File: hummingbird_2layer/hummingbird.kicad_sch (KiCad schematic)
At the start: 42 parts, among them J1 USB_C_Receptacle_USB2.0_16P, J2 srv1, J3 srv2, J4 halleffect, J5 Conn_01x06, J6 Conn_01x02, J7 Conn_01x02, J8 PWR_IN, J9 Conn_02x02_Counter_Clockwise, Q1 AO3400A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

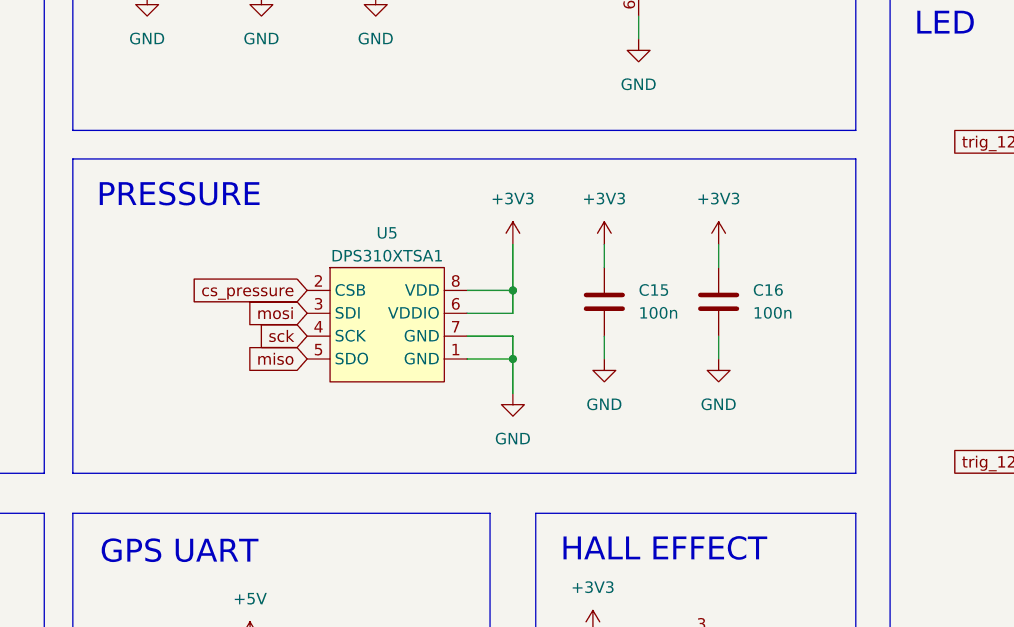
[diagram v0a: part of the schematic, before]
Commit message: backup before replacing sensor
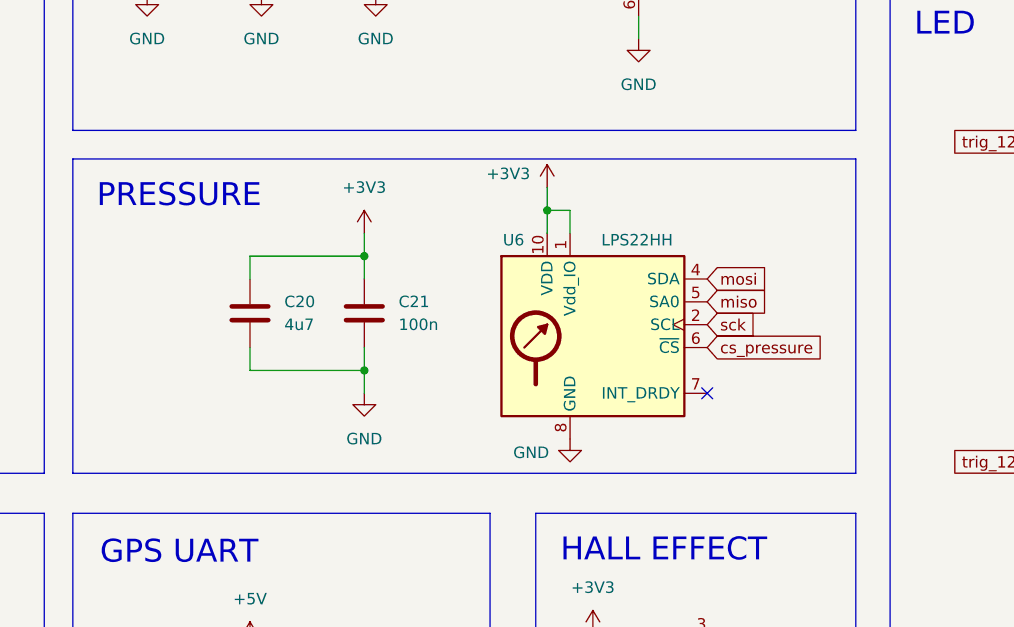
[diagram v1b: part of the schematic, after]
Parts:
- removed C15, C16: 100n, Capacitor_SMD:C_0402_1005Metric, symbol Device:C
- removed U5: DPS310XTSA1, Package_LGA:Bosch_LGA-8_2x2.5mm_P0.65mm_ClockwisePinNumbering, symbol symbols:DPS310
- added C20: 4u7, Capacitor_SMD:C_0402_1005Metric, symbol Device:C
- added C21: 100n, Capacitor_SMD:C_0402_1005Metric, symbol Device:C
- added U6: LPS22HH, Package_LGA:ST_HLGA-10_2x2mm_P0.5mm_LayoutBorder3x2y, symbol Sensor_Pressure:LPS22HH
- J5: LCSC C22461268 -> (none)
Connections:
- net +3V3: now also C20.1, C21.1, U6.1 (Vdd_IO), U6.10 (VDD)
- net GND: now also C20.2, C21.2, U6.3 (GND), U6.8 (GND), U6.9 (GND)
- net cs_pressure: now also U6.6 (~{CS})
- net miso: now also U6.5 (SA0)
- net mosi: now also U6.4 (SDA)
- net sck: now also U6.2 (SCL)
- no-connect marks 21 -> 22
